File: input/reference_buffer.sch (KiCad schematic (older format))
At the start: 12 parts, among them U1 OP27

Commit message: Mainly work on the top level of the input board, attaching signals to the channels, digital I/O.  Decided to use Eurocard 64 pin type B connector for the connection to the main board.  See input_board_pinout.txt.
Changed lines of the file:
@@
 EESchema Schematic File Version 4
-LIBS:reference_buffer-cache
+LIBS:input_board-cache
+LIBS:input_channel-cache
 EELAYER 29 0
 EELAYER END
 $Descr A4 11693 8268
 encoding utf-8
-Sheet 1 1
+Sheet 7 10
 Title ""
 Date ""
@@
 U 1 1 5DE453A9
 P 4000 1400
-F 0 "#PWR02" H 4000 1250 50  0001 C CNN
+F 0 "#PWR?" H 4000 1250 50  0001 C CNN
 F 1 "+15V" H 4015 1573 50  0000 C CNN
 F 2 "" H 4000 1400 50  0001 C CNN
@@
 $Comp
 L Device:C_Small C3
-U 1 1 5DE6EE08
+U 1 1 5DFFAD19
 P 4350 1500
-F 0 "C3" V 4121 1500 50  0000 C CNN
+F 0 "C?" V 4121 1500 50  0000 C CNN
 F 1 "1u" V 4212 1500 50  0000 C CNN
 F 2 "Capacitor_SMD:C_0603_1608Metric" H 4350 1500 50  0001 C CNN
@@
 $Comp
 L power:-15V #PWR03
-U 1 1 5DE6EE07
+U 1 1 5DFFAD18
 P 4000 2400
-F 0 "#PWR03" H 4000 2500 50  0001 C CNN
+F 0 "#PWR?" H 4000 2500 50  0001 C CNN
 F 1 "-15V" H 4015 2573 50  0000 C CNN
 F 2 "" H 4000 2400 50  0001 C CNN
@@
 U 1 1 5DE6EE09
 P 4600 1500
-F 0 "#PWR04" H 4600 1250 50  0001 C CNN
+F 0 "#PWR?" H 4600 1250 50  0001 C CNN
 F 1 "GNDA" V 4605 1372 50  0000 R CNN
 F 2 "" H 4600 1500 50  0001 C CNN
@@
 $Comp
 L Device:C_Small C4
-U 1 1 5DE6EE0A
+U 1 1 5DFFAD1B
 P 4350 2350
-F 0 "C4" V 4121 2350 50  0000 C CNN
+F 0 "C?" V 4121 2350 50  0000 C CNN
 F 1 "1u" V 4212 2350 50  0000 C CNN
 F 2 "Capacitor_SMD:C_0603_1608Metric" H 4350 2350 50  0001 C CNN
@@
 $Comp
 L power:GNDA #PWR05
-U 1 1 5DE6EE0B
+U 1 1 5DFFAD1C
 P 4600 2350
-F 0 "#PWR05" H 4600 2100 50  0001 C CNN
+F 0 "#PWR?" H 4600 2100 50  0001 C CNN
 F 1 "GNDA" V 4605 2222 50  0000 R CNN
 F 2 "" H 4600 2350 50  0001 C CNN
@@
 U 1 1 5DE44053
 P 3950 1900
-F 0 "U1" H 4294 1946 50  0000 L CNN
+F 0 "U?" H 4294 1946 50  0000 L CNN
 F 1 "OP27" H 4294 1855 50  0000 L CNN
 F 2 "" H 4000 1950 50  0001 C CNN
@@
 U 1 1 5DE6107D
 P 4150 3600
-F 0 "R4" V 4250 3600 50  0000 C CNN
+F 0 "R?" V 4250 3600 50  0000 C CNN
 F 1 "2K" V 4050 3600 50  0000 C CNN
 F 2 "Resistor_SMD:R_0603_1608Metric" V 4190 3590 50  0001 C CNN
@@
 U 1 1 5DEB4146
 P 4150 3150
-F 0 "C2" V 3921 3150 50  0000 C CNN
+F 0 "C?" V 3921 3150 50  0000 C CNN
 F 1 "47n" V 4012 3150 50  0000 C CNN
 F 2 "Capacitor_SMD:C_0603_1608Metric" H 4150 3150 50  0001 C CNN
@@
 U 1 1 5DEB8671
 P 5650 1900
-F 0 "R5" V 5750 1900 50  0000 C CNN
+F 0 "R?" V 5750 1900 50  0000 C CNN
 F 1 "100 mOhm" V 5550 1900 50  0000 C CNN
 F 2 "Resistor_SMD:R_0603_1608Metric" V 5690 1890 50  0001 C CNN
@@
 U 1 1 5DEBF53D
 P 2200 2300
-F 0 "R3" V 2300 2300 50  0000 C CNN
+F 0 "R?" V 2300 2300 50  0000 C CNN
 F 1 "2K" V 2100 2300 50  0000 C CNN
 F 2 "Resistor_SMD:R_0603_1608Metric" V 2240 2290 50  0001 C CNN
@@
 U 1 1 5DEBA857
 P 1750 3600
-F 0 "R2" V 1850 3600 50  0000 C CNN
+F 0 "R?" V 1850 3600 50  0000 C CNN
 F 1 "4.02K" V 1650 3600 50  0000 C CNN
 F 2 "Resistor_SMD:R_0603_1608Metric" V 1790 3590 50  0001 C CNN
@@
 U 1 1 5DEB389F
 P 1750 1800
-F 0 "R1" V 1850 1800 50  0000 C CNN
+F 0 "R?" V 1850 1800 50  0000 C CNN
 F 1 "4.02K" V 1650 1800 50  0000 C CNN
 F 2 "Resistor_SMD:R_0603_1608Metric" V 1790 1790 50  0001 C CNN
@@
 U 1 1 5DEC64D2
 P 2200 2650
-F 0 "#PWR01" H 2200 2400 50  0001 C CNN
+F 0 "#PWR?" H 2200 2400 50  0001 C CNN
 F 1 "GNDA" H 2300 2450 50  0000 R CNN
 F 2 "" H 2200 2650 50  0001 C CNN
@@
 U 1 1 5DEBFFBB
 P 2700 2300
-F 0 "C1" V 2850 2300 50  0000 C CNN
+F 0 "C?" V 2850 2300 50  0000 C CNN
 F 1 "47n" V 2562 2300 50  0000 C CNN
 F 2 "Capacitor_SMD:C_0603_1608Metric" H 2700 2300 50  0001 C CNN
@@
 U 1 1 5DEC8871
 P 6750 2250
-F 0 "C5" V 6900 2250 50  0000 C CNN
+F 0 "C?" V 6900 2250 50  0000 C CNN
 F 1 "47u" V 6612 2250 50  0000 C CNN
 F 2 "Capacitor_SMD:C_1210_3225Metric" H 6750 2250 50  0001 C CNN
@@
 U 1 1 5DEC962A
 P 6750 2550
-F 0 "#PWR06" H 6750 2300 50  0001 C CNN
+F 0 "#PWR?" H 6750 2300 50  0001 C CNN
 F 1 "GNDA" H 6850 2350 50  0000 R CNN
 F 2 "" H 6750 2550 50  0001 C CNN
@@
 U 1 1 5DECAF06
 P 7250 2250
-F 0 "C6" V 7400 2250 50  0000 C CNN
+F 0 "C?" V 7400 2250 50  0000 C CNN
 F 1 "47u" V 7112 2250 50  0000 C CNN
 F 2 "Capacitor_SMD:C_1210_3225Metric" H 7250 2250 50  0001 C CNN

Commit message: Still beating into overall shape.  This is a checkpoint before modifying the analog signal chain to fold the diff amp and antialias into the driver, going to a full differential path.
Overall: Changes to component attributes to reduce duplicates in BOM, and added links to Digikey and datasheets.

board_connector.sch: Added reference input pins, decimation SEL lines.

in_filter.sch:
Fixed BIST feedback to be taken at the top of each injection resistor (4 lines, not 2)

input_board.sch:
Added some missing connections and no-connects.

power_budget.xlsx:
Much more elaborate now, models effect of input levels on load currents, computes currents and total power, for several variants.

reference_buffer.sch:
Updated with booster sink transistor to handle sourcing into reference by ADC clamp diodes.

simetrix/:
Added supply_negative.wxsch and supply_positive.wxsch, which are concepts for low noise lowish dropout regulators for the analog rails.  Other simetrix modifications are cosmetic.
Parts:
- added D1, D2: BAV99, Package_TO_SOT_SMD:SOT-23, symbol Diode:BAV99
- added Q1: MJD32CG, Package_TO_SOT_SMD:TO-252-3_TabPin2, symbol Device:Q_PNP_BCE
- added R5, R8: 499, Resistor_SMD:R_1206_3216Metric, symbol Device:R_US
- added R6: 2.74, Resistor_SMD:R_1206_3216Metric, symbol Device:R_US
- C1, C2: value 47n -> 10nF; footprint Capacitor_SMD:C_0603_1608Metric -> Capacitor_SMD:C_0805_2012Metric; Description (none) -> CAP CER 10000PF 50V C0G/NP0 0805; Digikey (none) -> 490-8296-1-ND; MPN (none) -> GRM2195C1H103GA01D; Notes (none) -> 2% C0G
- C3, C4: value 1u -> 1uF
- C5, C6: value 47u -> 47uF
- R1, R2, R3, R4: footprint Resistor_SMD:R_0603_1608Metric -> Resistor_SMD:R_0805_2012Metric
- R5: value 100 mOhm -> 68m; footprint Resistor_SMD:R_0603_1608Metric -> Resistor_SMD:R_1206_3216Metric
- U1: footprint (none) -> Package_SO:SOIC-8_3.9x4.9mm_P1.27mm
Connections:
- wire segments 42 -> 61
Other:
- note added: "C5, C6 at the output (same part as at the ADCs)\nform a tee filter with the decoupling inductors at the \nADC on each channel to minimize cross-coupling\nof noise between the ADCs. LTC documents that\nthis is a problem, though suggests buying one\nof their references per-ADC to solve it."
- note added: "Reference buffer"
- note added: "The buffer is normally biased into class-A operation by R5, which supplies\n10 mA. The total draw expected on the reference bus is about 5 mA. This\nbias keeps Q1 on so that it is ready to clamp overvoltage. D2 allows\nthe opamp to source extra current into the reference bus if needed,\nup to the opamp current limit.\n\nD2/R6 set a sink current limit of about 300 mA. This prevents\n400 uF of low-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"
- note added: "The reference needs to be able to sink perhaps as much as 150 mA if all \nthree channels are driven into saturation, because the ADC driver output\nexceeds VREF, which is used as the clamp voltage for the analog inputs. \nThen each driver is in current limit until the situation resolves. Overdrive on\nall channels is easy to get in normal operation, just move the sensor close \nto the source.\n\n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"
- note removed: "The capacitors at the output (same as at the ADCs)\nform a tee filter with the decoupling inductors on \neach channel to minimize cross-coupling of noise\nbetween the ADCs."
- moved on the sheet: C2, C3, C4, C5, C6, R1, R2, R3, R4, R7, U3

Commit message: Changes mostly related to avoiding excess power consumption.  This is mainly by limiting the signal swing to 0..5V and using asymmetric supplies of -4V and +8V.  (Perhaps we can reduce these to 3/7 V.)  Also, I got rid of two stages in the input signal path.
power_budget.xlsx
power.sch
reference_buffer.sch:
Changes related to the new supply voltages, and start on the power supply section.

input_channel.sch
in_amp.sch
antialias_driver.sch:
Reworked the input signal chain to keep a full differential path, rolling the antialias filter
into the ADC driver.  Also, related to change to lower asymmetrical supply voltages, there is
no 20V PP anywhere (the this was for benefit of the antialias filter noise, but that stage is gone).  Also, added zener clamp on VREF in driver.

in_filter.sch: added missing DC bias resistors.
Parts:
- removed R8: 499, Resistor_SMD:R_1206_3216Metric, symbol Device:R_US
- D1, D2: value BAV99 -> BAS21S
- R1, R2: value 4.02K -> 2K
- R5: value 499 -> 200; Description RES 499 OHM 0.1% 2/5W 1206 -> (none); Digikey 541-3877-1-ND -> (none)
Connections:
- net labels added: V+, V-, VREF
- net labels removed: +15V, -15V, reference
- wire segments 61 -> 58
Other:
- note added: "The buffer is normally biased into class-A operation by R5, which supplies\n15 mA. The total draw expected on the reference bus is about 5 mA. This\nbias keeps Q1 on so that it is ready to clamp overvoltage. D2 allows\nthe opamp to source extra current into the reference bus if needed,\nup to the opamp current limit.\n\nD2/R6 set a sink current limit of about 300 mA. This prevents\n400 uF of low-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"
- note added: "The reference buffer receives the 5V reference from the edge connector\nand buffers it for the large capacitive load of the reference bypass caps. \nThe reference comes in differentially so as to re-reference the voltage to the gound\npresent on the input card, mimizing effect of DC and low-frequency ground shifts.\n\nThe bandwidth of the reference is approximately 4.5 kHz, which helps to reject\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"
- note removed: "The buffer is normally biased into class-A operation by R5, which supplies\n10 mA. The total draw expected on the reference bus is about 5 mA. This\nbias keeps Q1 on so that it is ready to clamp overvoltage. D2 allows\nthe opamp to source extra current into the reference bus if needed,\nup to the opamp current limit.\n\nD2/R6 set a sink current limit of about 300 mA. This prevents\n400 uF of low-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"
- note removed: "The reference buffer receives the differential reference from the edge connector\nand buffers it for the large capacitive load of the reference bypass caps. The buffer\nis gain of 1/2, since we need a 5V reference for the ADCs, but we distribute the \nreference as 10V to maximize the accuracy in distribution on the main board. \nThe reference comes in differentially so as to re-reference the volt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"

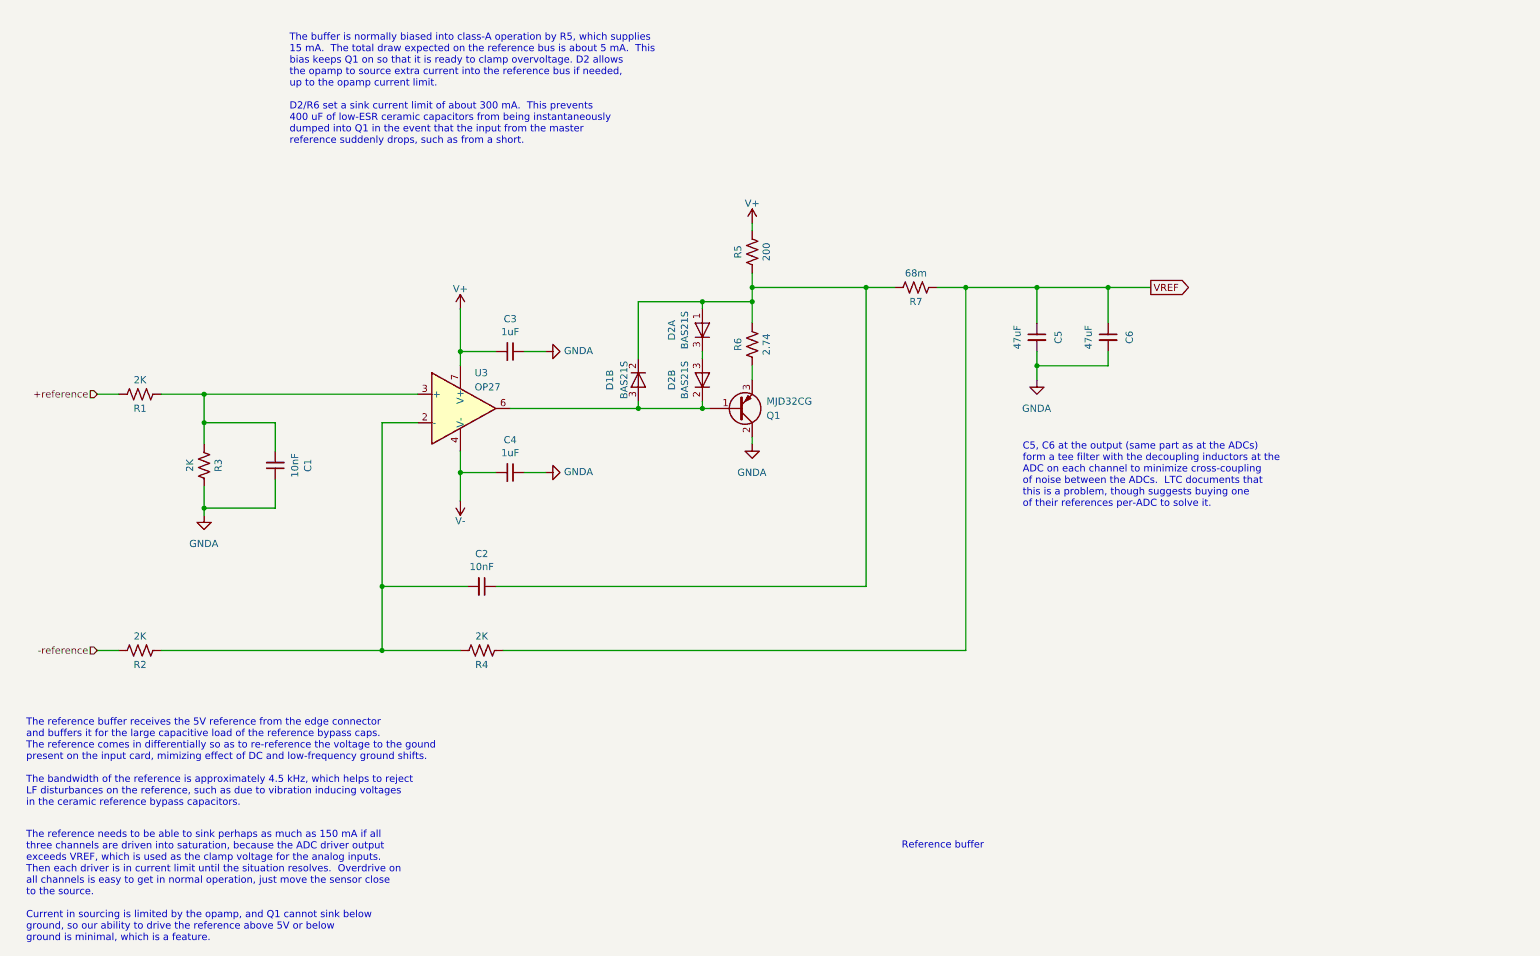
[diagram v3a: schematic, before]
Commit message: Mostly work on power, regulators and distribution.  Also more BOM cleanup.
All of the bypass capacitors are now spec'd and in the DigiKey BOM. TVS zeners are now
spec'd.  Folded together some resistor values and got rid of some 1206 parts that no longer
need that much power rating at the lower supplies.

A affecting all of the input channel sheets is that we now distribute filtered V+, V- and VREF
via sheet ports.  The V+, V- filter is on input_channel.sch and the VREF filter is still in
adc.sch, but is distributed out to the other sheets that need it.

bist_buffer.sch: added buffer for built-in self-test

board_connector.sch: put the input filter for the analog supplies here.

power.sch: added regulators for the supplies.

reference_buffer.sch:
changed components to match those chosen for the V+, V- regulators and added
current steering diodes to bootstrap the reference buffer supply.  This is
necessary because the analog supplies are now derived from VREF.

*.wxsch:
Updates to spice models related to work on supplies.
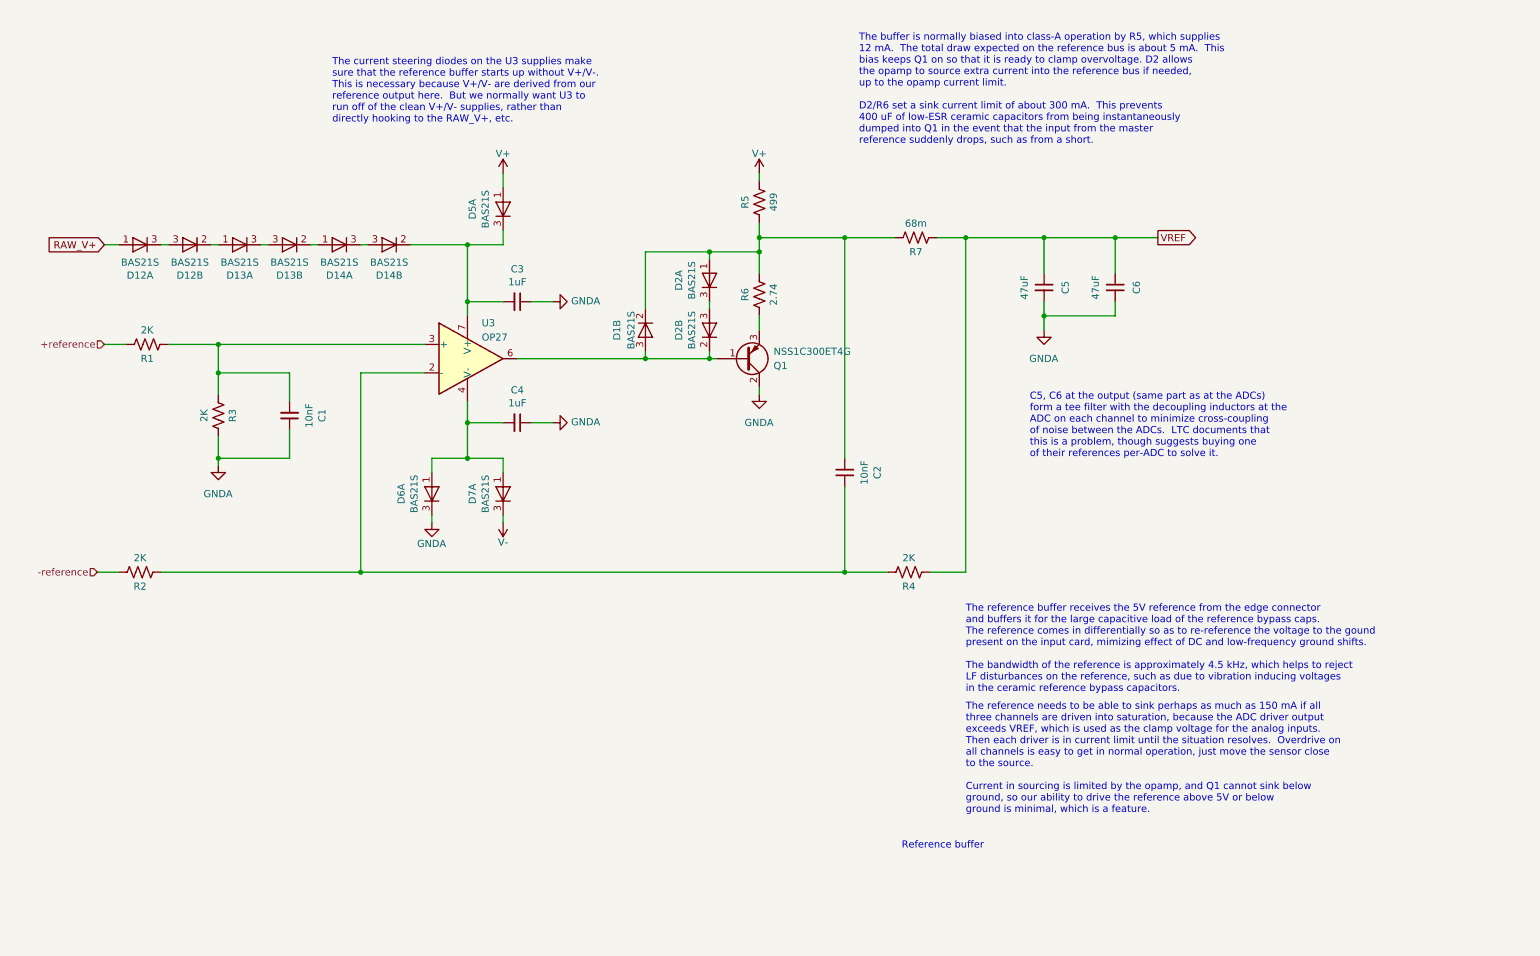
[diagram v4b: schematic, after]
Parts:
- added D12, D13, D14, D5, D6, D7: BAS21S, Package_TO_SOT_SMD:SOT-23, symbol Diode:BAV99
- C3, C4: footprint Capacitor_SMD:C_0603_1608Metric -> Capacitor_SMD:C_0805_2012Metric; Description (none) -> CAP CER 1UF 16V X7R 0805; Digikey (none) -> 1276-6471-1-ND; MPN (none) -> CL21B105KOFNNNG
- C5, C6: Description (none) -> CAP CER 47UF 6.3V X7R 1210; Digikey (none) -> 399-5516-1-ND; MPN (none) -> C1210C476M9RACTU
- Q1: value MJD32CG -> NSS1C300ET4G; Description (none) -> TRANS PNP 100V 3A 3DPAK; Digikey (none) -> NSS1C300ET4GOSCT-ND
- R5: value 200 -> 499; footprint Resistor_SMD:R_1206_3216Metric -> Resistor_SMD:R_0805_2012Metric; Description (none) -> RES SMD 499 OHM 0.1% 1/4W 0805; Digikey (none) -> A110514CT-ND; Notes (none) -> 0.1%
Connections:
- net GNDA: now also D6.3 (K)
- net V+: now also D5.1 (A); no longer C3.2, U1.7 (V+)
- net V-: now also D7.3 (K); no longer C4.2, U1.4 (V-)
- net at R2.1, R4.2, U1.2 (-): now also C2.1; no longer C2.2
- net at D1.1 (A), D2.2 (K), R5.1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: now also C2.2; no longer C2.1
- new net: C4.2, D6.1 (A), D7.1 (A), U1.4 (V-)
- new net: C3.2, D14.2 (K), D5.3 (K), U1.7 (V+)
- new net: D12.3 (A), D12.3 (K)
- new net: D12.2 (K), D13.1 (A)
- new net: D13.3 (A), D13.3 (K)
- new net: D13.2 (K), D14.1 (A)
- new net: D14.3 (A), D14.3 (K)
- new net RAW_V+: D12.1 (A)
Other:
- note added: "The buffer is normally biased into class-A operation by R5, which supplies\n12 mA. The total draw expected on the reference bus is about 5 mA. This\nbias keeps Q1 on so that it is ready to clamp overvoltage. D2 allows\nthe opamp to source extra current into the reference bus if needed,\nup to the opamp current limit.\n\nD2/R6 set a sink current limit of about 300 mA. This prevents\n400 uF of low-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"
- note added: "The current steering diodes on the U3 supplies make\nsure that the reference buffer starts up without V+/V-.\nThis is necessary because V+/V- are derived from our\nreference output here. But we normally want U3 to\nrun off of the clean V+/V- supplies, rather than\ndirectly hooking to the RAW_V+, etc."
- note removed: "The buffer is normally biased into class-A operation by R5, which supplies\n15 mA. The total draw expected on the reference bus is about 5 mA. This\nbias keeps Q1 on so that it is ready to clamp overvoltage. D2 allows\nthe opamp to source extra current into the reference bus if needed,\nup to the opamp current limit.\n\nD2/R6 set a sink current limit of about 300 mA. This prevents\n400 uF of low-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"
- moved on the sheet: C1, C2, C3, C4, C5, C6, D1B, D2A, D2B, Q1, R1, R2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

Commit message: Mostly finished wiring.
Finished mapping pins in board_connector.sch.  Renamed some nets and moved the analog
supply filter to power.sch.  Added probe_connector.sch which now includes input protected
on the probe calibration one-wire line.  The configuration digital interface stuff is still
sketchy, this is basically a placeholder.  Eventually we will have an I2C I/O extender for
configuration and calibration memory, but for now I added a jumper header for setting the
SEL0/SEL1 lines to control the ADC decimation.
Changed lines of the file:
@@
 $Descr A4 11693 8268
 encoding utf-8
-Sheet 10 12
+Sheet 10 13
 Title ""
 Date ""
@@
 $EndComp
 Wire Wire Line
-	1500 3150 1650 3150
+	1450 3150 1650 3150
 Wire Wire Line
 	1450 4750 1600 4750
-Text HLabel 1450 4750 0    50   Input ~ 0
--reference
 $Comp
 L Device:R_US R2
@@
 	0    1    1    0
 $EndComp
-Text HLabel 1500 3150 0    50   Input ~ 0
-+reference
 Wire Wire Line
 	2300 3150 2300 3350
@@
 Wire Wire Line
 	3650 2450 4050 2450
+Text GLabel 1450 3150 0    50   Input ~ 0
++reference
+Text GLabel 1450 4750 0    50   Input ~ 0
+-reference
 $EndSCHEMATC
